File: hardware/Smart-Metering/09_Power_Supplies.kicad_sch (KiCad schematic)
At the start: 0 parts

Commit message: Implementa folha de alimentação do domínio seguro
09_Power_Supplies (tudo referenciado a GND_SYS):

- entrada 5 V por OU de diodos Schottky: VIN_ACDC (conversor AC/DC da
  folha 01) e VBUS (USB-C de serviço);
- U901 BQ24074: carregador Li-ion 1S com power path; ILIM ≈ 1,48 A,
  carga ≈ 0,89 A, NTC do pack em TS, ~PGOOD/~CHG para o MCU;
- U902 TPS63021: buck-boost de VSYS para +3V3 (opera em toda a faixa
  da bateria);
- U903 TPS61023: boost de VSYS para +5V (alimenta o DC/DC isolado da
  folha 06 e cargas de 5 V da HMI);
- SW901 desliga os conversores via PWR_EN; divisor VBAT_SENSE = VBAT/2.

Novos símbolos: D_Schottky, L_Horiz, SW_SPST, Conn_01x03, BQ24074,
TPS63021 e TPS61023 (pinouts a conferir; numeração de TPS63021 e
TPS61023 provisória). O gerador passa a aceitar labels locais.

Co-Authored-By: Claude Opus 5.5 <noreply@anthropic.com>
Claude-Session: https://claude.ai/code/session_012B8cVkhtjf3eg98UdpNCpf
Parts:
- added C901, C902, C905, C908: 10uF, Capacitor_SMD:C_0805_2012Metric, symbol SmartMetering:C_Vert
- added C903: 4.7uF, Capacitor_SMD:C_0805_2012Metric, symbol SmartMetering:C_Vert
- added C904: 100nF, Capacitor_SMD:C_0603_1608Metric, symbol SmartMetering:C_Vert
- added C906, C907, C909, C910: 22uF, Capacitor_SMD:C_1206_3216Metric, symbol SmartMetering:C_Vert
- added D901, D902: SS34, Diode_SMD:D_SMA, symbol SmartMetering:D_Schottky
- added J901: BATTERY_1S, symbol SmartMetering:Conn_01x03
- added L901: 1.5uH, symbol SmartMetering:L_Horiz
- added L902: 1uH, symbol SmartMetering:L_Horiz
- added R901: 1k, Resistor_SMD:R_0603_1608Metric, symbol SmartMetering:R_Vert
- added R902: 1.05k, Resistor_SMD:R_0603_1608Metric, symbol SmartMetering:R_Vert
- added R903: 46.4k, Resistor_SMD:R_0603_1608Metric, symbol SmartMetering:R_Vert
- added R904, R905: 10k, Resistor_SMD:R_0603_1608Metric, symbol SmartMetering:R_Vert
- added R906, R907, R908, R910: 100k, Resistor_SMD:R_0603_1608Metric, symbol SmartMetering:R_Vert
- added R909: 732k, Resistor_SMD:R_0603_1608Metric, symbol SmartMetering:R_Vert
- added SW901: POWER, symbol SmartMetering:SW_SPST
- added U901: BQ24074, symbol SmartMetering:BQ24074
- added U902: TPS63021, symbol SmartMetering:TPS63021
- added U903: TPS61023, symbol SmartMetering:TPS61023
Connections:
- new net: L901.1, U902.7 (L1)
- new net: L901.2, U902.5 (L2)
- new net: L902.2, U903.5 (SW)
- new net +3V3: C906.1, C907.1, R904.1, R905.1, U902.3 (FB), U902.4 (VOUT)
- new net +5V: C909.1, C910.1, R909.1, U903.6 (VOUT)
- new net BAT_NTC: J901.2, U901.1 (TS)
- new net CHG_N: R905.2, U901.9 (~{CHG})
- new net FB_5V: R909.2, R910.1, U903.1 (FB)
- new net GND_SYS: C901.2, C902.2, C903.2, C904.2, C905.2, C906.2, C907.2, C908.2, C909.2, C910.2, J901.3, R901.2, R902.2, R903.2, R907.2, R910.2, SW901.2, U901.15 (SYSOFF), U901.17 (EP), U901.4 (~{CE}), U901.5 (EN2), U901.8 (VSS), U902.2 (GND), U902.6 (PGND), U903.4 (GND)
- new net ILIM: R902.1, U901.12 (ILIM)
- new net ISET: R901.1, U901.16 (ISET)
- new net PGOOD_N: R904.2, U901.7 (~{PGOOD})
- new net PG_3V3: U902.11 (PG)
- new net PWR_EN: R908.2, SW901.1, U902.9 (EN), U903.2 (EN)
- new net TMR: R903.1, U901.14 (TMR)
- new net VBAT: C903.1, J901.1, R906.1, U901.2 (BAT), U901.3 (BAT)
- new net VBAT_SENSE: C904.1, R906.2, R907.1
- new net VBUS: D902.2 (A)
- new net VIN_ACDC: D901.2 (A)
- new net VIN_CHG: C901.1, D901.1 (K), D902.1 (K), U901.13 (IN)
- new net VSYS: C902.1, C905.1, C908.1, L902.1, R908.1, U901.10 (OUT), U901.11 (OUT), U901.6 (EN1), U902.1 (VINA), U902.10 (PS/SYNC), U902.8 (VIN), U903.3 (VIN)
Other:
- note added: "ALIMENTAÇÃO DO DOMÍNIO SEGURO (GND_SYS) VIN_ACDC (5 V, conversor AC/DC da folha 01) --D901--+ VBUS (USB-C de serviço, folha 08) ----------D902--+--> VIN_CHG -> U901 BQ24074 U901 OUT = VSYS (alimenta o sistema com ou sem bateria; carrega a bateria com o excedente) VSYS -> U902 TPS63021 (buck-boost) -> +3V3 | VSYS -> U903 TPS61023 (boost) -> +5V +5V alimenta PS601 (DC/DC isolado da folha 06) e carg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"
- note added: "CARREGADOR U901 EN1 = 1, EN2 = 0 -> limite de entrada definido por R902 (≈ 1,48 A) R901: corrente de carga ≈ 0,89 A (bateria 1S >= 2500 mAh -> <= 0,4 C) TS: NTC de 10 kΩ do pack (J901 pino 2). ~CE e SYSOFF em GND: sempre habilitado. ~PGOOD / ~CHG: estado para o MCU (coletor aberto, pull-up em +3V3). VBAT_SENSE = VBAT / 2 para o ADC do MCU."
- note added: "ORÇAMENTO DE POTÊNCIA (estimativa a refinar) ESP32-P4 + ESP32-C6 + PHY Ethernet + MCU ~1,5 W Display 7" com backlight ~2,5 W Domínio metrológico via PS601 ~0,5 W Total ~4,5 W -> ~1,3 A da bateria a 3,6 V; ~1,5 h com 2500 mAh. Com rede presente o AC/DC supre o sistema; a bateria é reserva para registrar interrupções e para uso portátil."
- note added: "SW901: fechada desliga os conversores (PWR_EN = 0). Futuramente pode virar liga/desliga controlado pelo MCU. ATENÇÃO: pinouts de BQ24074 (de memória) e numeração de pinos de TPS63021 e TPS61023 (provisória) DEVEM ser conferidos nos datasheets antes do layout. Layout dos conversores: seguir o layout recomendado (laço de comutação curto)."
- company: (none) -> Smart-Metering
- title: (none) -> Power Supplies - Safe Domain

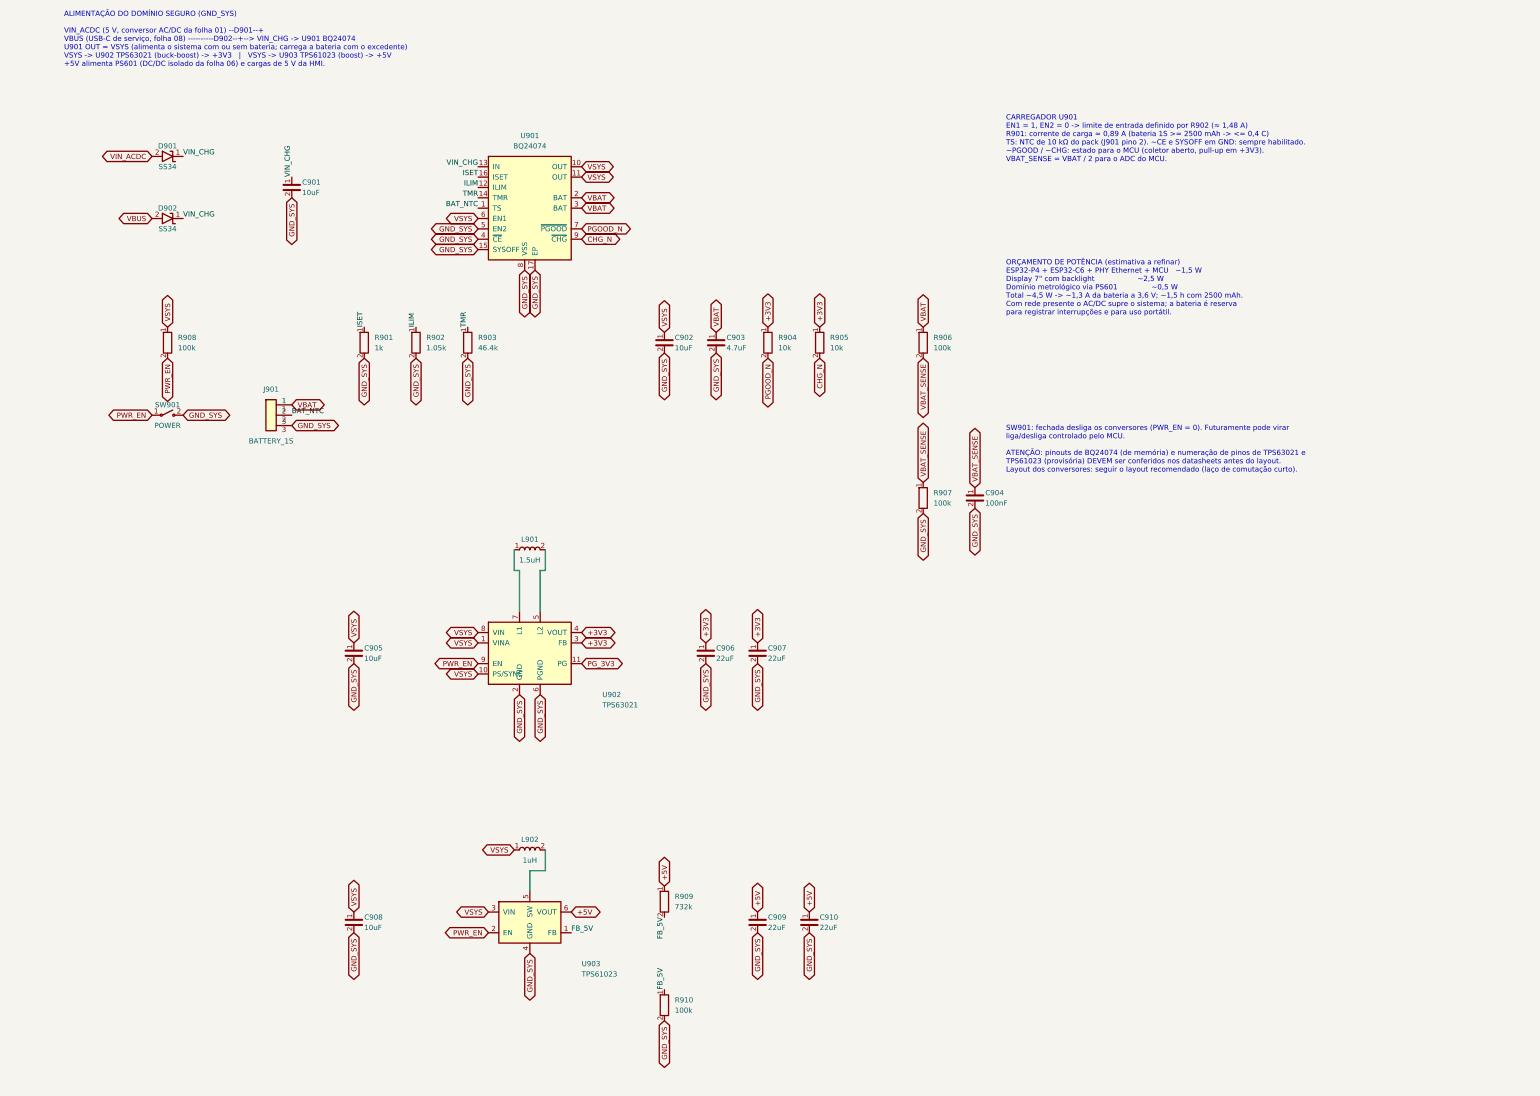
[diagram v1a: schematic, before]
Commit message: Usa símbolos oficiais do KiCad nas folhas de isolação e alimentação
Os símbolos oficiais da biblioteca KiCad 10 (gitlab.com/kicad/libraries)
substituem os desenhados de memória:

- 06_Isolation: ISO7762DW (4/2) e ISO7761DW (5/1) no lugar de três
  ISO774x; os 12 sinais cabem em dois isoladores reforçados. MCP3204 e
  TPS7A20xxxDBV oficiais (os pinouts anteriores conferiram).
- 09_Power_Supplies: BQ24074RGT oficial revelou que o pino 15 é ITERM,
  não SYSOFF; agora tem R911 (3,01 kΩ, fim de carga ≈ 90 mA). +3V3 passa
  ao TPS63001 (buck-boost 3,3 V fixo) e +5V ao TPS61089, com resistores
  de frequência, limite de corrente e compensação a confirmar no WEBENCH.

Símbolos próprios que deixaram de ser usados foram removidos da
biblioteca SmartMetering.

Co-Authored-By: Claude Opus 5.5 <noreply@anthropic.com>
Claude-Session: https://claude.ai/code/session_012B8cVkhtjf3eg98UdpNCpf
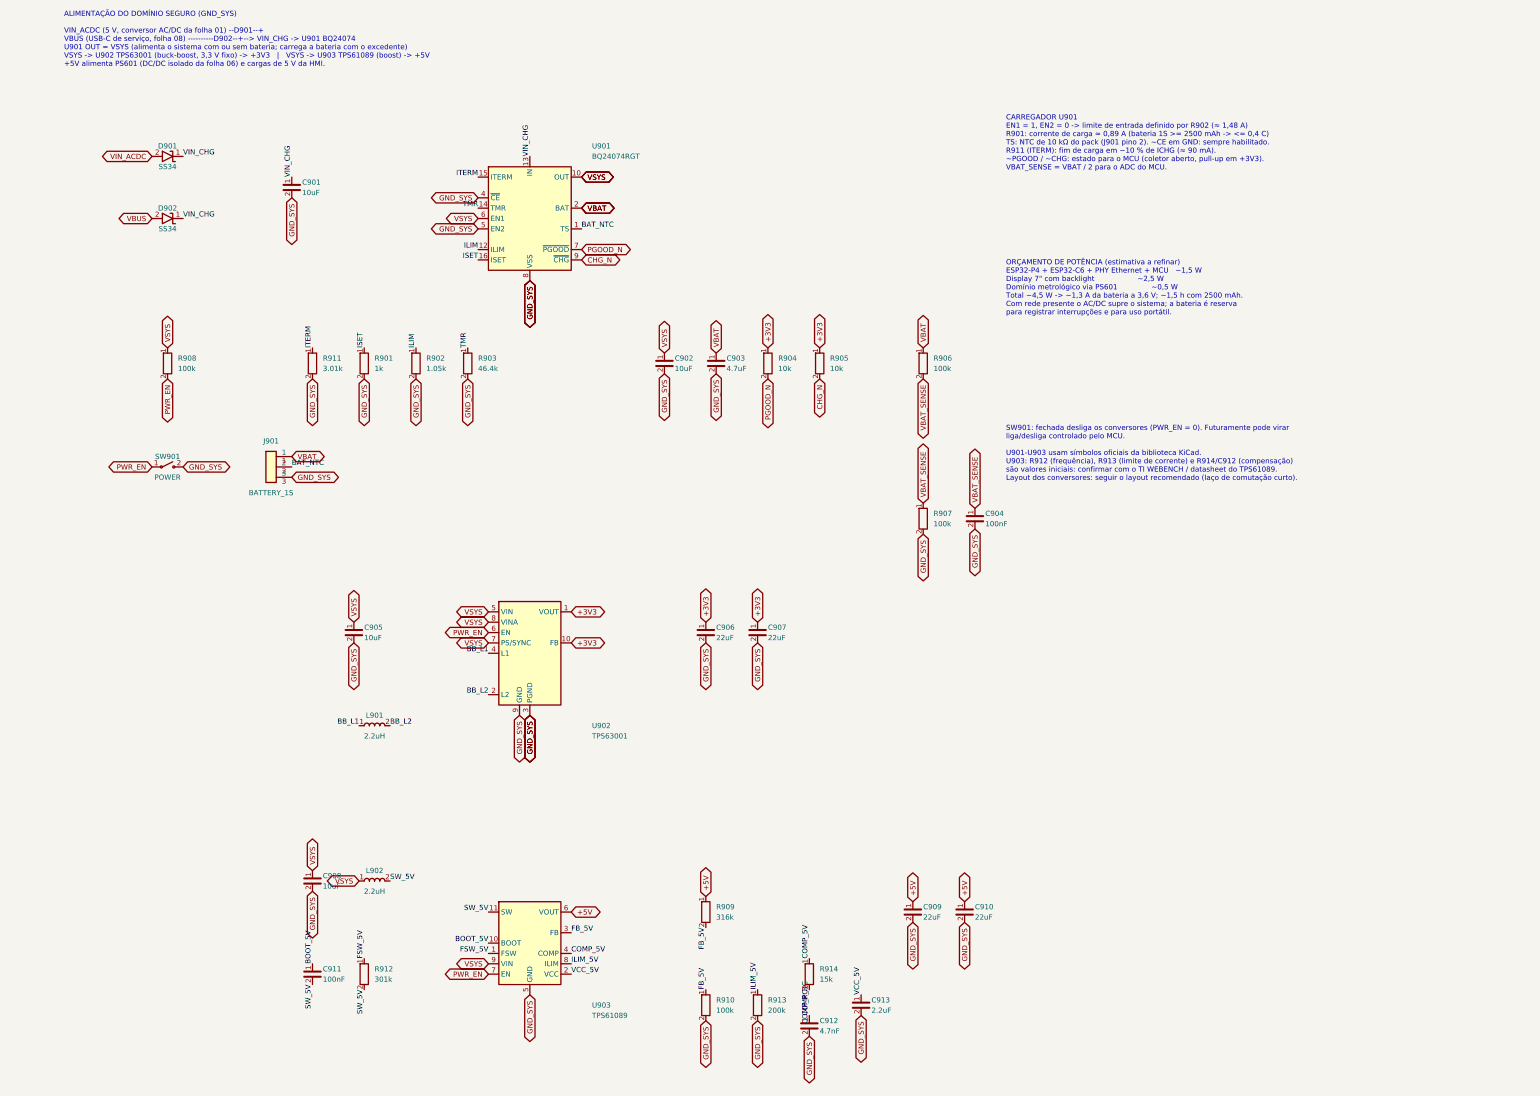
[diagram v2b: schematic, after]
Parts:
- removed U901: BQ24074, symbol SmartMetering:BQ24074
- removed U902: TPS63021, symbol SmartMetering:TPS63021
- removed U903: TPS61023, symbol SmartMetering:TPS61023
- added C911: 100nF, Capacitor_SMD:C_0603_1608Metric, symbol SmartMetering:C_Vert
- added C912: 4.7nF, Capacitor_SMD:C_0603_1608Metric, symbol SmartMetering:C_Vert
- added C913: 2.2uF, Capacitor_SMD:C_0603_1608Metric, symbol SmartMetering:C_Vert
- added R911: 3.01k, Resistor_SMD:R_0603_1608Metric, symbol SmartMetering:R_Vert
- added R912: 301k, Resistor_SMD:R_0603_1608Metric, symbol SmartMetering:R_Vert
- added R913: 200k, Resistor_SMD:R_0603_1608Metric, symbol SmartMetering:R_Vert
- added R914: 15k, Resistor_SMD:R_0603_1608Metric, symbol SmartMetering:R_Vert
- added U901: BQ24074RGT, Package_DFN_QFN:VQFN-16-1EP_3x3mm_P0.5mm_EP1.6x1.6mm, symbol Battery_Management:BQ24074RGT
- added U902: TPS63001, Package_SON:Texas_DRC0010J_ThermalVias, symbol Regulator_Switching:TPS63001
- added U903: TPS61089, Package_DFN_QFN:Texas_VQFN-RNR0011A-11, symbol Regulator_Switching:TPS61089
- J901: footprint (none) -> Connector_JST:JST_PH_B3B-PH-K_1x03_P2.00mm_Vertical
- L901: value 1.5uH -> 2.2uH
- L902: value 1uH -> 2.2uH
- R909: value 732k -> 316k
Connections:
- net +3V3: now also U902.1 (VOUT), U902.10 (FB)
- net +5V: now also U903.6 (VOUT)
- net BAT_NTC: now also U901.1 (TS)
- net CHG_N: now also U901.9 (~{CHG})
- net FB_5V: now also U903.3 (FB)
- net GND_SYS: now also C912.2, C913.2, R911.2, R913.2, U901.17 (VSS), U901.4 (~{CE}), U901.5 (EN2), U901.8 (VSS), U902.11 (PGND), U902.3 (PGND), U902.9 (GND), U903.5 (GND)
- net ILIM: now also U901.12 (ILIM)
- net ISET: now also U901.16 (ISET)
- net PGOOD_N: now also U901.7 (~{PGOOD})
- net PWR_EN: now also U902.6 (EN), U903.7 (EN)
- net TMR: now also U901.14 (TMR)
- net VBAT: now also U901.2 (BAT), U901.3 (BAT)
- net VIN_CHG: now also U901.13 (IN)
- net VSYS: now also U901.10 (OUT), U901.11 (OUT), U901.6 (EN1), U902.5 (VIN), U902.7 (PS/SYNC), U902.8 (VINA), U903.9 (VIN)
- net BB_L1: now reaches L901.1
- net BB_L1: now also U902.4 (L1)
- net BB_L2: now reaches L901.2
- net BB_L2: now also U902.2 (L2)
- net SW_5V: now reaches L902.2
- net SW_5V: now also C911.2, R912.2, U903.11 (SW)
- new net BOOT_5V: C911.1, U903.10 (BOOT)
- new net COMP_5V: R914.1, U903.4 (COMP)
- new net COMP_RC: C912.1, R914.2
- new net FSW_5V: R912.1, U903.1 (FSW)
- new net ILIM_5V: R913.1, U903.8 (ILIM)
- new net ITERM: R911.1, U901.15 (ITERM)
- new net VCC_5V: C913.1, U903.2 (VCC)
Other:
- note added: "ALIMENTAÇÃO DO DOMÍNIO SEGURO (GND_SYS) VIN_ACDC (5 V, conversor AC/DC da folha 01) --D901--+ VBUS (USB-C de serviço, folha 08) ----------D902--+--> VIN_CHG -> U901 BQ24074 U901 OUT = VSYS (alimenta o sistema com ou sem bateria; carrega a bateria com o excedente) VSYS -> U902 TPS63001 (buck-boost, 3,3 V fixo) -> +3V3 | VSYS -> U903 TPS61089 (boost) -> +5V +5V alimenta PS601 (DC/DC isolado da folh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"
- note added: "CARREGADOR U901 EN1 = 1, EN2 = 0 -> limite de entrada definido por R902 (≈ 1,48 A) R901: corrente de carga ≈ 0,89 A (bateria 1S >= 2500 mAh -> <= 0,4 C) TS: NTC de 10 kΩ do pack (J901 pino 2). ~CE em GND: sempre habilitado. R911 (ITERM): fim de carga em ~10 % de ICHG (≈ 90 mA). ~PGOOD / ~CHG: estado para o MCU (coletor aberto, pull-up em +3V3). VBAT_SENSE = VBAT / 2 para o ADC do MCU."
- note added: "SW901: fechada desliga os conversores (PWR_EN = 0). Futuramente pode virar liga/desliga controlado pelo MCU. U901-U903 usam símbolos oficiais da biblioteca KiCad. U903: R912 (frequência), R913 (limite de corrente) e R914/C912 (compensação) são valores iniciais: confirmar com o TI WEBENCH / datasheet do TPS61089. Layout dos conversores: seguir o layout recomendado (laço de comutação curto)."
- note removed: "ALIMENTAÇÃO DO DOMÍNIO SEGURO (GND_SYS) VIN_ACDC (5 V, conversor AC/DC da folha 01) --D901--+ VBUS (USB-C de serviço, folha 08) ----------D902--+--> VIN_CHG -> U901 BQ24074 U901 OUT = VSYS (alimenta o sistema com ou sem bateria; carrega a bateria com o excedente) VSYS -> U902 TPS63021 (buck-boost) -> +3V3 | VSYS -> U903 TPS61023 (boost) -> +5V +5V alimenta PS601 (DC/DC isolado da folha 06) e carg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"
- note removed: "CARREGADOR U901 EN1 = 1, EN2 = 0 -> limite de entrada definido por R902 (≈ 1,48 A) R901: corrente de carga ≈ 0,89 A (bateria 1S >= 2500 mAh -> <= 0,4 C) TS: NTC de 10 kΩ do pack (J901 pino 2). ~CE e SYSOFF em GND: sempre habilitado. ~PGOOD / ~CHG: estado para o MCU (coletor aberto, pull-up em +3V3). VBAT_SENSE = VBAT / 2 para o ADC do MCU."
- note removed: "SW901: fechada desliga os conversores (PWR_EN = 0). Futuramente pode virar liga/desliga controlado pelo MCU. ATENÇÃO: pinouts de BQ24074 (de memória) e numeração de pinos de TPS63021 e TPS61023 (provisória) DEVEM ser conferidos nos datasheets antes do layout. Layout dos conversores: seguir o layout recomendado (laço de comutação curto)."
